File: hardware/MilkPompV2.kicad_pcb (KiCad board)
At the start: 2 copper layers, 160 x 67.3 mm, 67 parts, among them J1 OUTPUTS, J2 Conn_Display, J3 Program_Conn, J4 Conn_02x07_Odd_Even, J6 PWR INPUT, K1 G5LE-1, Q1 BC847, Q2 BC847, SW1 SW_IO, SW2 SW_IO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

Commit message: project name added
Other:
- board text added: "MilkPomp"
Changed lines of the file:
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@@
   (gr_line (start 176.53 133.35) (end 176.53 123.952) (layer "Edge.Cuts") (width 0.1))
   (gr_line (start 176.53 118.872) (end 176.53 103.378) (layer "Edge.Cuts") (width 0.1))
+  (gr_text "MilkPomp" (at 109.22 113.03) (layer "F.Cu")
+    (effects (font (size 1.5 1.5) (thickness 0.3) italic))
+  )
   (segment (start 128.02 79.252) (end 128.27 79.502) (width 0.5) (layer "F.Cu") (net 1))
   (segment (start 186.69 88.2904) (end 186.69 87.63) (width 0.8) (layer "F.Cu") (net 1))

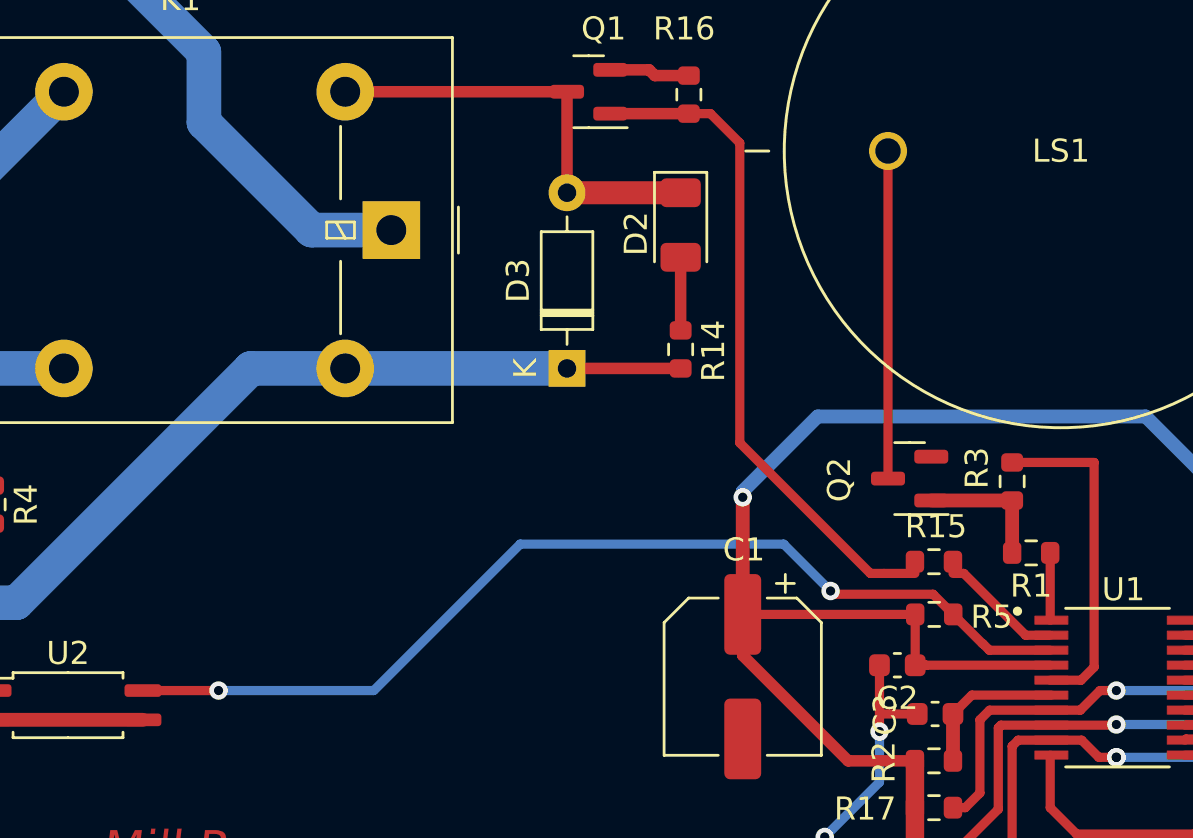
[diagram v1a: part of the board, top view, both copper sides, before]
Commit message: PCB arranged
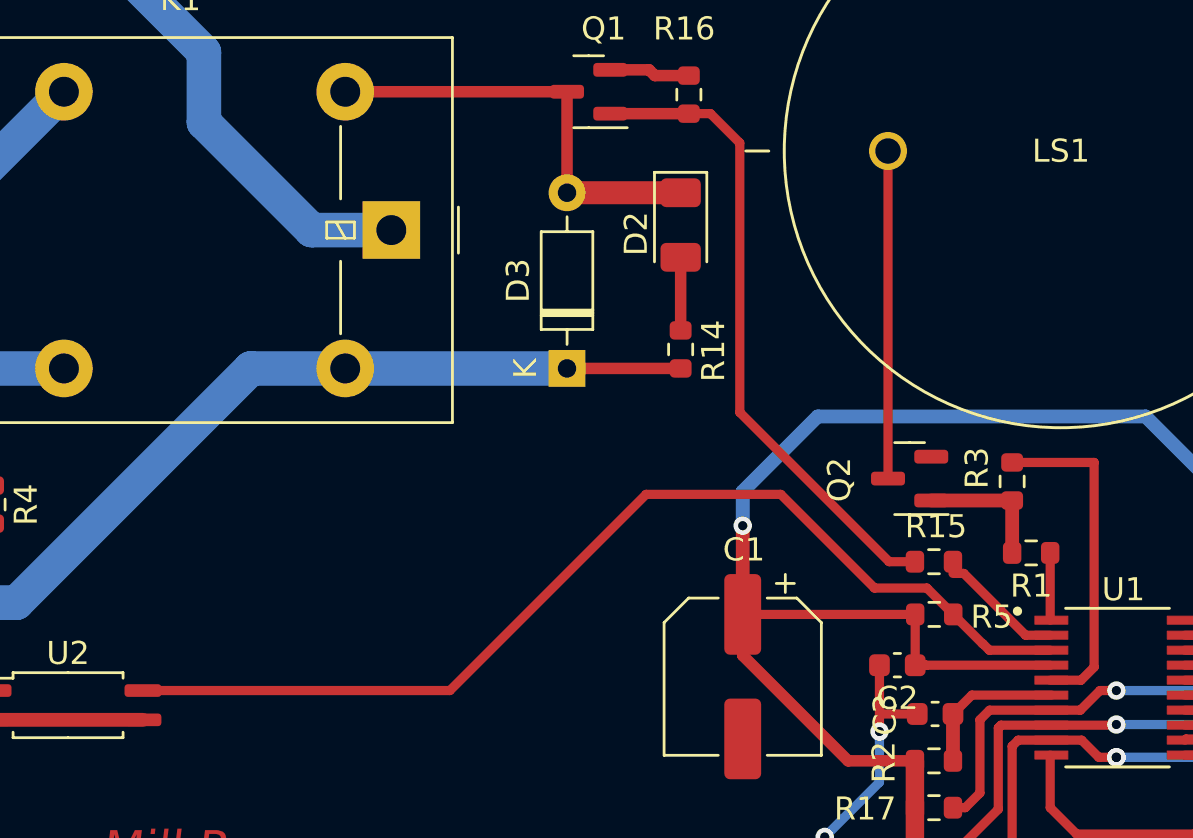
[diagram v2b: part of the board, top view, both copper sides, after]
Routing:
- net FLOW: track 43.9 -> 45.7 mm, vias 2 -> 0
- net Net-(Q1-Pad1): track 29.1 -> 28.1 mm
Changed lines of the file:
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@@
   (segment (start 140.036199 105.073801) (end 139.5208 105.073801) (width 0.4) (layer "F.Cu") (net 2))
   (segment (start 140.462 117.348) (end 139.5486 116.4346) (width 0.8) (layer "F.Cu") (net 2))
+  (segment (start 132.08 99.0225) (end 132.08 102.87) (width 0.6) (layer "F.Cu") (net 2))
   (segment (start 142.875 117.348) (end 140.462 117.348) (width 0.8) (layer "F.Cu") (net 2))
   (segment (start 139.5608 102.87) (end 132.08 102.87) (width 0.4) (layer "F.Cu") (net 2))
   (segment (start 139.5608 102.87) (end 139.5608 105.073801) (width 0.4) (layer "F.Cu") (net 2))
-  (segment (start 132.08 97.79) (end 132.08 102.87) (width 0.6) (layer "F.Cu") (net 2))
   (segment (start 145.0523 121.6152) (end 148.2527 121.6152) (width 0.4) (layer "F.Cu") (net 2))
   (segment (start 143.764 116.459) (end 142.875 117.348) (width 0.8) (layer "F.Cu") (net 2))
@@
   (segment (start 145.415 105.073801) (end 140.036199 105.073801) (width 0.4) (layer "F.Cu") (net 2))
   (segment (start 140.036199 105.073801) (end 139.5608 105.073801) (width 0.4) (layer "F.Cu") (net 2))
-  (via (at 132.08 97.79) (size 0.8) (drill 0.4) (layers "F.Cu" "B.Cu") (net 2))
+  (via (at 132.08 99.0225) (size 0.8) (drill 0.4) (layers "F.Cu" "B.Cu") (net 2))
+  (segment (start 149.5552 94.2848) (end 151.7904 96.52) (width 0.6) (layer "B.Cu") (net 2))
   (segment (start 156.21 91.44) (end 153.3815 88.6115) (width 0.6) (layer "B.Cu") (net 2))
   (segment (start 163.83 96.52) (end 156.21 96.52) (width 0.6) (layer "B.Cu") (net 2))
-  (segment (start 149.5552 94.2848) (end 151.7904 96.52) (width 0.6) (layer "B.Cu") (net 2))
+  (segment (start 132.08 99.0225) (end 132.08 97.536) (width 0.6) (layer "B.Cu") (net 2))
+  (segment (start 151.7904 96.52) (end 156.21 96.52) (width 0.6) (layer "B.Cu") (net 2))
   (segment (start 153.3815 88.6115) (end 153.3815 82.773) (width 0.6) (layer "B.Cu") (net 2))
+  (segment (start 156.21 96.52) (end 156.21 91.44) (width 0.6) (layer "B.Cu") (net 2))
   (segment (start 135.3312 94.2848) (end 149.5552 94.2848) (width 0.6) (layer "B.Cu") (net 2))
   (segment (start 132.08 97.536) (end 135.3312 94.2848) (width 0.6) (layer "B.Cu") (net 2))
-  (segment (start 132.08 97.79) (end 132.08 97.536) (width 0.6) (layer "B.Cu") (net 2))
-  (segment (start 156.21 96.52) (end 156.21 91.44) (width 0.6) (layer "B.Cu") (net 2))
-  (segment (start 151.7904 96.52) (end 156.21 96.52) (width 0.6) (layer "B.Cu") (net 2))
   (segment (start 146.722201 107.023799) (end 142.785201 107.023799) (width 0.4) (layer "F.Cu") (net 3))
   (segment (start 159.8168 102.4128) (end 167.5892 102.4128) (width 0.4) (layer "F.Cu") (net 3))
@@
   (segment (start 158.75 97.917) (end 158.75 91.44) (width 0.4) (layer "F.Cu") (net 16))
   (segment (start 145.415 103.1238) (end 145.415 100.203) (width 0.4) (layer "F.Cu") (net 17))
+  (segment (start 131.953 82.423) (end 130.682 81.152) (width 0.4) (layer "F.Cu") (net 18))
+  (segment (start 126.335 81.152) (end 129.7432 81.152) (width 0.5) (layer "F.Cu") (net 18))
+  (segment (start 138.43 100.584) (end 131.953 94.107) (width 0.4) (layer "F.Cu") (net 18))
+  (segment (start 139.5486 100.584) (end 138.43 100.584) (width 0.4) (layer "F.Cu") (net 18))
+  (segment (start 131.953 94.107) (end 131.953 82.423) (width 0.4) (layer "F.Cu") (net 18))
   (segment (start 130.682 81.152) (end 129.7432 81.152) (width 0.4) (layer "F.Cu") (net 18))
-  (segment (start 126.335 81.152) (end 129.7432 81.152) (width 0.5) (layer "F.Cu") (net 18))
-  (segment (start 139.5486 101.092) (end 138.2052 101.092) (width 0.4) (layer "F.Cu") (net 18))
-  (segment (start 138.2052 101.092) (end 137.6172 101.092) (width 0.4) (layer "F.Cu") (net 18))
-  (segment (start 131.953 95.4278) (end 131.953 82.423) (width 0.4) (layer "F.Cu") (net 18))
-  (segment (start 137.6172 101.092) (end 131.953 95.4278) (width 0.4) (layer "F.Cu") (net 18))
-  (segment (start 131.953 82.423) (end 130.682 81.152) (width 0.4) (layer "F.Cu") (net 18))
   (segment (start 99.568 98.932) (end 99.568 106.172) (width 0.5) (layer "F.Cu") (net 19))
-  (segment (start 142.4808 104.14) (end 142.494 104.14) (width 0.4) (layer "F.Cu") (net 20))
-  (segment (start 109.347 106.172) (end 106.068 106.172) (width 0.4) (layer "F.Cu") (net 20))
-  (segment (start 142.777799 104.423799) (end 145.415 104.423799) (width 0.4) (layer "F.Cu") (net 20))
-  (segment (start 140.3358 101.995) (end 142.4808 104.14) (width 0.4) (layer "F.Cu") (net 20))
-  (segment (start 136.031 101.995) (end 140.3358 101.995) (width 0.4) (layer "F.Cu") (net 20))
-  (segment (start 135.89 101.854) (end 136.031 101.995) (width 0.4) (layer "F.Cu") (net 20))
-  (segment (start 142.494 104.14) (end 142.777799 104.423799) (width 0.4) (layer "F.Cu") (net 20))
-  (via (at 109.347 106.172) (size 0.8) (drill 0.4) (layers "F.Cu" "B.Cu") (net 20))
-  (via (at 135.89 101.854) (size 0.8) (drill 0.4) (layers "F.Cu" "B.Cu") (net 20))
-  (segment (start 122.428 99.822) (end 116.078 106.172) (width 0.4) (layer "B.Cu") (net 20))
-  (segment (start 133.858 99.822) (end 122.428 99.822) (width 0.4) (layer "B.Cu") (net 20))
-  (segment (start 116.078 106.172) (end 109.347 106.172) (width 0.4) (layer "B.Cu") (net 20))
-  (segment (start 135.89 101.854) (end 133.858 99.822) (width 0.4) (layer "B.Cu") (net 20))
+  (segment (start 127.889 97.663) (end 119.38 106.172) (width 0.4) (layer "F.Cu") (net 20))
+  (segment (start 142.4808 104.14) (end 140.0678 101.727) (width 0.4) (layer "F.Cu") (net 20))
+  (segment (start 119.38 106.172) (end 106.068 106.172) (width 0.4) (layer "F.Cu") (net 20))
+  (segment (start 142.494 104.14) (end 142.4808 104.14) (width 0.4) (layer "F.Cu") (net 20))
+  (segment (start 137.795 101.727) (end 133.731 97.663) (width 0.4) (layer "F.Cu") (net 20))
+  (segment (start 145.415 104.423799) (end 142.777799 104.423799) (width 0.4) (layer "F.Cu") (net 20))
+  (segment (start 133.731 97.663) (end 127.889 97.663) (width 0.4) (layer "F.Cu") (net 20))
+  (segment (start 142.777799 104.423799) (end 142.494 104.14) (width 0.4) (layer "F.Cu") (net 20))
+  (segment (start 140.0678 101.727) (end 137.795 101.727) (width 0.4) (layer "F.Cu") (net 20))
   (segment (start 236.1575 106.7525) (end 236.1575 111.252) (width 0.8) (layer "F.Cu") (net 21))
   (segment (start 233.6175 106.7525) (end 233.6175 111.252) (width 0.8) (layer "F.Cu") (net 22))
